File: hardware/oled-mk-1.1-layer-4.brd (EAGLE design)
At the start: 72 x 34 mm, 0 parts

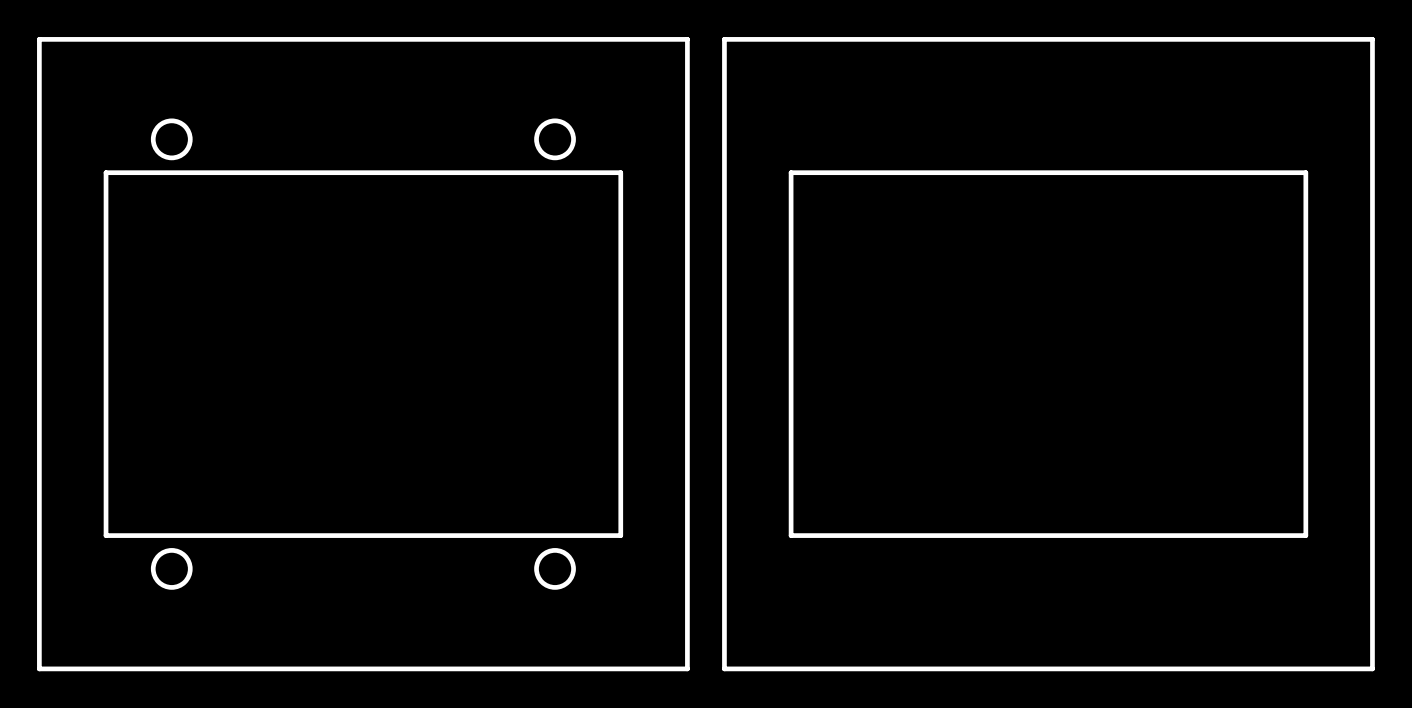
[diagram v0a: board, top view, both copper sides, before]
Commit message: layout for laser cutting
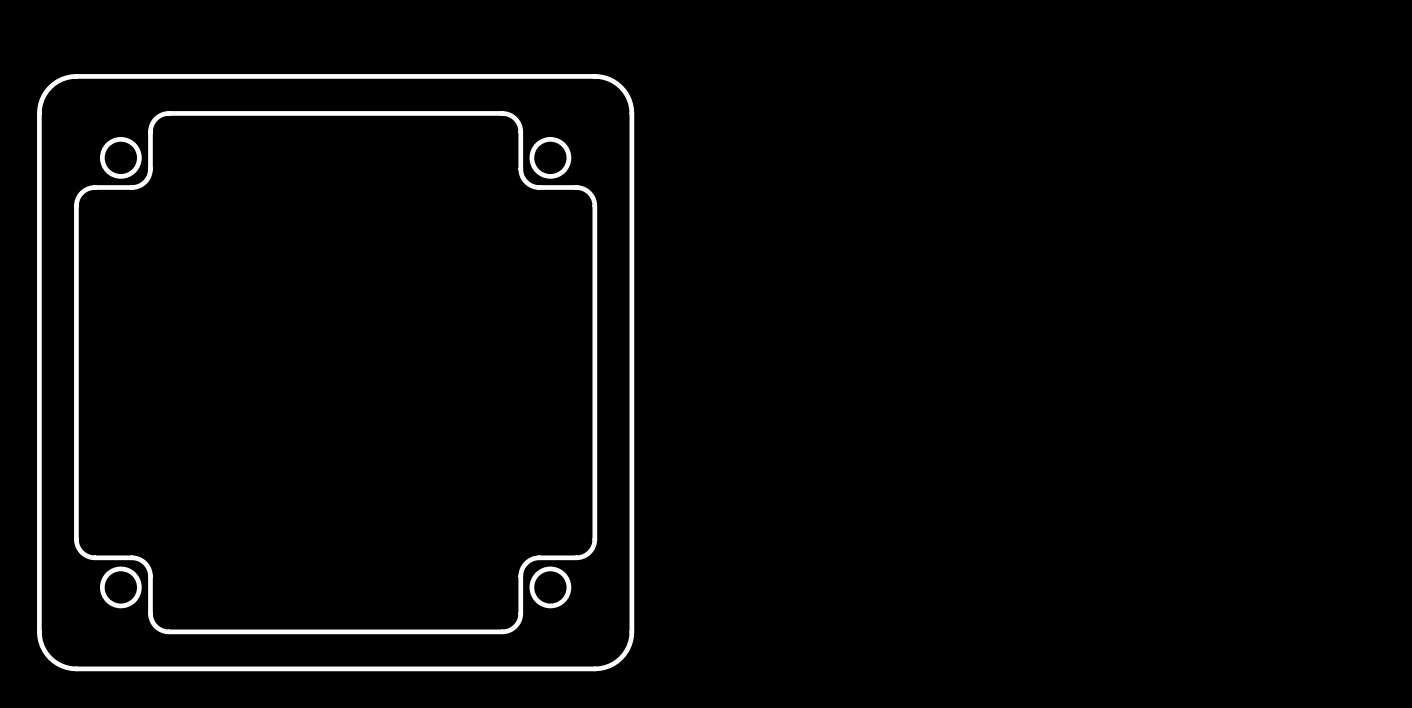
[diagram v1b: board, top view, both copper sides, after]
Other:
- board size 72 x 34 mm -> 32 x 32 mm
- board text added: "1.00 in calibration sq"
- board text added: "Layer 4 Opaque Blue Acrylic (1.5mm)"
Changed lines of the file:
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@@
 <layer number="44" name="Drills" color="7" fill="1" visible="no" active="yes"/>
 <layer number="45" name="Holes" color="7" fill="1" visible="yes" active="yes"/>
-<layer number="46" name="Milling" color="3" fill="1" visible="no" active="yes"/>
-<layer number="47" name="Measures" color="7" fill="1" visible="yes" active="yes"/>
+<layer number="46" name="Milling" color="3" fill="1" visible="yes" active="yes"/>
+<layer number="47" name="Measures" color="14" fill="1" visible="yes" active="yes"/>
 <layer number="48" name="Document" color="7" fill="1" visible="yes" active="yes"/>
 <layer number="49" name="Reference" color="7" fill="1" visible="yes" active="yes"/>
-<layer number="51" name="tDocu" color="7" fill="1" visible="yes" active="yes"/>
+<layer number="51" name="tDocu" color="3" fill="1" visible="yes" active="yes"/>
 <layer number="52" name="bDocu" color="5" fill="1" visible="yes" active="yes"/>
 </layers>
 <board>
 <plain>
-<wire x1="0" y1="34" x2="35" y2="34" width="0.254" layer="20"/>
-<wire x1="35" y1="34" x2="35" y2="0" width="0.254" layer="20"/>
-<wire x1="35" y1="0" x2="0" y2="0" width="0.254" layer="20"/>
-<wire x1="0" y1="0" x2="0" y2="34" width="0.254" layer="20"/>
-<wire x1="3.85" y1="30.65" x2="3.85" y2="3.35" width="0.1524" layer="51"/>
-<wire x1="3.85" y1="3.35" x2="31.15" y2="3.35" width="0.1524" layer="51"/>
-<wire x1="31.15" y1="3.35" x2="31.15" y2="30.65" width="0.1524" layer="51"/>
-<wire x1="31.15" y1="30.65" x2="3.85" y2="30.65" width="0.1524" layer="51"/>
-<wire x1="3.85" y1="7.5" x2="31.15" y2="7.5" width="0.1524" layer="52"/>
-<wire x1="3.85" y1="26.5" x2="31.15" y2="26.5" width="0.1524" layer="52"/>
-<wire x1="3.85" y1="7.5" x2="3.85" y2="26.5" width="0.1524" layer="52"/>
-<wire x1="31.15" y1="26.5" x2="31.15" y2="7.5" width="0.1524" layer="52"/>
-<wire x1="3.6" y1="7.2" x2="3.6" y2="26.8" width="0.254" layer="20"/>
-<wire x1="31.4" y1="7.2" x2="31.4" y2="26.8" width="0.254" layer="20"/>
-<wire x1="31.4" y1="26.8" x2="3.6" y2="26.8" width="0.254" layer="20"/>
-<wire x1="31.4" y1="7.2" x2="3.6" y2="7.2" width="0.254" layer="20"/>
-<circle x="7.15" y="28.6" radius="1" width="0.254" layer="20"/>
-<circle x="27.85" y="28.6" radius="1" width="0.254" layer="20"/>
-<circle x="27.85" y="5.4" radius="1" width="0.254" layer="20"/>
-<circle x="7.15" y="5.4" radius="1" width="0.254" layer="20"/>
-<wire x1="37" y1="34" x2="72" y2="34" width="0.254" layer="20"/>
-<wire x1="72" y1="34" x2="72" y2="0" width="0.254" layer="20"/>
-<wire x1="72" y1="0" x2="37" y2="0" width="0.254" layer="20"/>
-<wire x1="37" y1="0" x2="37" y2="34" width="0.254" layer="20"/>
-<wire x1="40.6" y1="7.2" x2="40.6" y2="26.8" width="0.254" layer="20"/>
-<wire x1="68.4" y1="7.2" x2="68.4" y2="26.8" width="0.254" layer="20"/>
-<wire x1="68.4" y1="26.8" x2="40.6" y2="26.8" width="0.254" layer="20"/>
-<wire x1="68.4" y1="7.2" x2="40.6" y2="7.2" width="0.254" layer="20"/>
-<wire x1="40.85" y1="30.65" x2="40.85" y2="3.35" width="0.1524" layer="51"/>
-<wire x1="40.85" y1="3.35" x2="68.15" y2="3.35" width="0.1524" layer="51"/>
-<wire x1="68.15" y1="3.35" x2="68.15" y2="30.65" width="0.1524" layer="51"/>
-<wire x1="68.15" y1="30.65" x2="40.85" y2="30.65" width="0.1524" layer="51"/>
+<wire x1="30" y1="0" x2="2" y2="0" width="0.254" layer="46"/>
+<wire x1="2" y1="0" x2="0" y2="2" width="0.254" layer="46" curve="-90"/>
+<wire x1="0" y1="2" x2="0" y2="30" width="0.254" layer="46"/>
+<wire x1="0" y1="30" x2="2" y2="32" width="0.254" layer="46" curve="-90"/>
+<wire x1="2" y1="32" x2="30" y2="32" width="0.254" layer="46"/>
+<wire x1="30" y1="32" x2="32" y2="30" width="0.254" layer="46" curve="-90"/>
+<wire x1="32" y1="30" x2="32" y2="2" width="0.254" layer="46"/>
+<wire x1="32" y1="2" x2="30" y2="0" width="0.254" layer="46" curve="-90"/>
+<circle x="4.4" y="27.6" radius="1" width="0.254" layer="46"/>
+<circle x="27.6" y="27.6" radius="1" width="0.254" layer="46"/>
+<circle x="27.6" y="4.4" radius="1" width="0.254" layer="46"/>
+<circle x="4.4" y="4.4" radius="1" width="0.254" layer="46"/>
+<wire x1="50.8" y1="25.4" x2="50.8" y2="0" width="0.1524" layer="47"/>
+<wire x1="50.8" y1="0" x2="76.2" y2="0" width="0.1524" layer="47"/>
+<wire x1="76.2" y1="0" x2="76.2" y2="25.4" width="0.1524" layer="47"/>
+<wire x1="76.2" y1="25.4" x2="50.8" y2="25.4" width="0.1524" layer="47"/>
+<text x="64" y="12.7" size="1.27" layer="47" font="vector" ratio="12" align="center">1.00 in
+calibration sq</text>
+<text x="16" y="35" size="1.27" layer="48" font="vector" ratio="12" align="center">Layer 4
+Opaque Blue Acrylic (1.5mm)</text>
+<rectangle x1="2.35" y1="2.35" x2="29.65" y2="29.65" layer="43"/>
+<rectangle x1="2.35" y1="6.5" x2="29.65" y2="25.5" layer="40"/>
+<wire x1="30" y1="0" x2="2" y2="0" width="0.05" layer="20"/>
+<wire x1="2" y1="0" x2="0" y2="2" width="0.05" layer="20" curve="-90"/>
+<wire x1="0" y1="2" x2="0" y2="30" width="0.05" layer="20"/>
+<wire x1="0" y1="30" x2="2" y2="32" width="0.05" layer="20" curve="-90"/>
+<wire x1="2" y1="32" x2="30" y2="32" width="0.05" layer="20"/>
+<wire x1="30" y1="32" x2="32" y2="30" width="0.05" layer="20" curve="-90"/>
+<wire x1="32" y1="30" x2="32" y2="2" width="0.05" layer="20"/>
+<wire x1="32" y1="2" x2="30" y2="0" width="0.05" layer="20" curve="-90"/>
+<circle x="4.4" y="27.6" radius="1" width="0.05" layer="20"/>
+<circle x="27.6" y="27.6" radius="1" width="0.05" layer="20"/>
+<circle x="27.6" y="4.4" radius="1" width="0.05" layer="20"/>
+<circle x="4.4" y="4.4" radius="1" width="0.05" layer="20"/>
+<wire x1="2" y1="7" x2="2" y2="25" width="0.05" layer="20"/>
+<wire x1="2" y1="25" x2="3" y2="26" width="0.05" layer="20" curve="-90"/>
+<wire x1="3" y1="26" x2="5" y2="26" width="0.05" layer="20"/>
+<wire x1="5" y1="26" x2="6" y2="27" width="0.05" layer="20" curve="90"/>
+<wire x1="6" y1="27" x2="6" y2="29" width="0.05" layer="20"/>
+<wire x1="6" y1="29" x2="7" y2="30" width="0.05" layer="20" curve="-90"/>
+<wire x1="7" y1="30" x2="25" y2="30" width="0.05" layer="20"/>
+<wire x1="25" y1="30" x2="26" y2="29" width="0.05" layer="20" curve="-90"/>
+<wire x1="26" y1="29" x2="26" y2="27" width="0.05" layer="20"/>
+<wire x1="26" y1="27" x2="27" y2="26" width="0.05" layer="20" curve="90"/>
+<wire x1="27" y1="26" x2="29" y2="26" width="0.05" layer="20"/>
+<wire x1="29" y1="26" x2="30" y2="25" width="0.05" layer="20" curve="-90"/>
+<wire x1="30" y1="25" x2="30" y2="7" width="0.05" layer="20"/>
+<wire x1="30" y1="7" x2="29" y2="6" width="0.05" layer="20" curve="-90"/>
+<wire x1="29" y1="6" x2="27" y2="6" width="0.05" layer="20"/>
+<wire x1="27" y1="6" x2="26" y2="5" width="0.05" layer="20" curve="90"/>
+<wire x1="26" y1="5" x2="26" y2="3" width="0.05" layer="20"/>
+<wire x1="26" y1="3" x2="25" y2="2" width="0.05" layer="20" curve="-90"/>
+<wire x1="25" y1="2" x2="7" y2="2" width="0.05" layer="20"/>
+<wire x1="7" y1="2" x2="6" y2="3" width="0.05" layer="20" curve="-90"/>
+<wire x1="6" y1="3" x2="6" y2="5" width="0.05" layer="20"/>
+<wire x1="6" y1="5" x2="5" y2="6" width="0.05" layer="20" curve="90"/>
+<wire x1="5" y1="6" x2="3" y2="6" width="0.05" layer="20"/>
+<wire x1="3" y1="6" x2="2" y2="7" width="0.05" layer="20" curve="-90"/>
+<wire x1="2" y1="7" x2="2" y2="25" width="0.254" layer="46"/>
+<wire x1="2" y1="25" x2="3" y2="26" width="0.254" layer="46" curve="-90"/>
+<wire x1="3" y1="26" x2="5" y2="26" width="0.254" layer="46"/>
+<wire x1="5" y1="26" x2="6" y2="27" width="0.254" layer="46" curve="90"/>
+<wire x1="6" y1="27" x2="6" y2="29" width="0.254" layer="46"/>
+<wire x1="6" y1="29" x2="7" y2="30" width="0.254" layer="46" curve="-90"/>
+<wire x1="7" y1="30" x2="25" y2="30" width="0.254" layer="46"/>
+<wire x1="25" y1="30" x2="26" y2="29" width="0.254" layer="46" curve="-90"/>
+<wire x1="26" y1="29" x2="26" y2="27" width="0.254" layer="46"/>
+<wire x1="26" y1="27" x2="27" y2="26" width="0.254" layer="46" curve="90"/>
+<wire x1="27" y1="26" x2="29" y2="26" width="0.254" layer="46"/>
+<wire x1="29" y1="26" x2="30" y2="25" width="0.254" layer="46" curve="-90"/>
+<wire x1="30" y1="25" x2="30" y2="7" width="0.254" layer="46"/>
+<wire x1="30" y1="7" x2="29" y2="6" width="0.254" layer="46" curve="-90"/>
+<wire x1="29" y1="6" x2="27" y2="6" width="0.254" layer="46"/>
+<wire x1="27" y1="6" x2="26" y2="5" width="0.254" layer="46" curve="90"/>
+<wire x1="26" y1="5" x2="26" y2="3" width="0.254" layer="46"/>
+<wire x1="26" y1="3" x2="25" y2="2" width="0.254" layer="46" curve="-90"/>
+<wire x1="25" y1="2" x2="7" y2="2" width="0.254" layer="46"/>
+<wire x1="7" y1="2" x2="6" y2="3" width="0.254" layer="46" curve="-90"/>
+<wire x1="6" y1="3" x2="6" y2="5" width="0.254" layer="46"/>
+<wire x1="6" y1="5" x2="5" y2="6" width="0.254" layer="46" curve="90"/>
+<wire x1="5" y1="6" x2="3" y2="6" width="0.254" layer="46"/>
+<wire x1="3" y1="6" x2="2" y2="7" width="0.254" layer="46" curve="-90"/>
 </plain>
 <attributes>
@@
 </board>
 </drawing>
+<compatibility>
+<note version="6.3" minversion="6.2.2" severity="warning">
+Since Version 6.2.2 text objects can contain more than one line,
+which will not be processed correctly with this version.
+</note>
+</compatibility>
 </eagle>
